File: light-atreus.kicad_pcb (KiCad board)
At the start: 2 copper layers, 40.1 x 37.5 mm, 10 parts, among them J1 USB_B, J11 USB_B, J2 CONN_01X02, J3 CONN_01X02, J4 CONN_01X02, J5 CONN_01X02, J6 CONN_01X02, J7 CONN_01X02, J8 CONN_01X02, J9 CONN_01X02

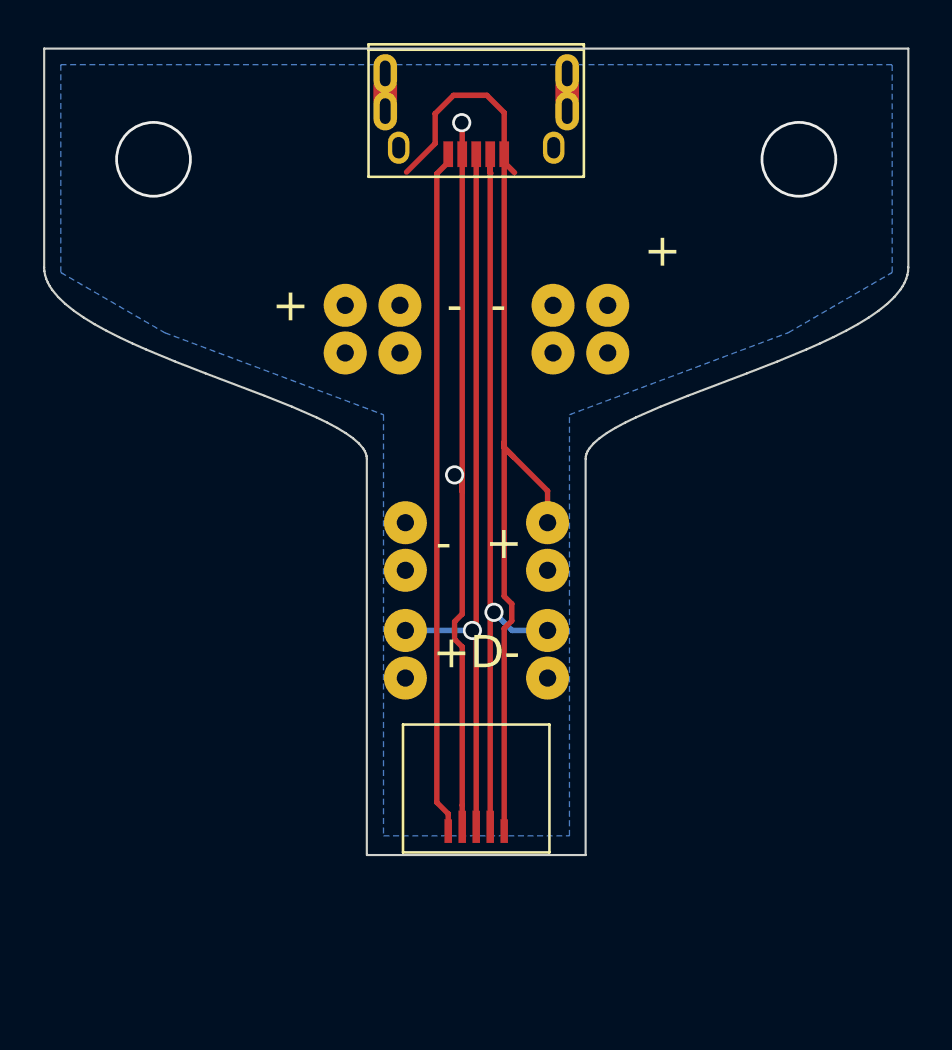
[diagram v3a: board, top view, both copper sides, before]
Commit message: Route last two V+ traces
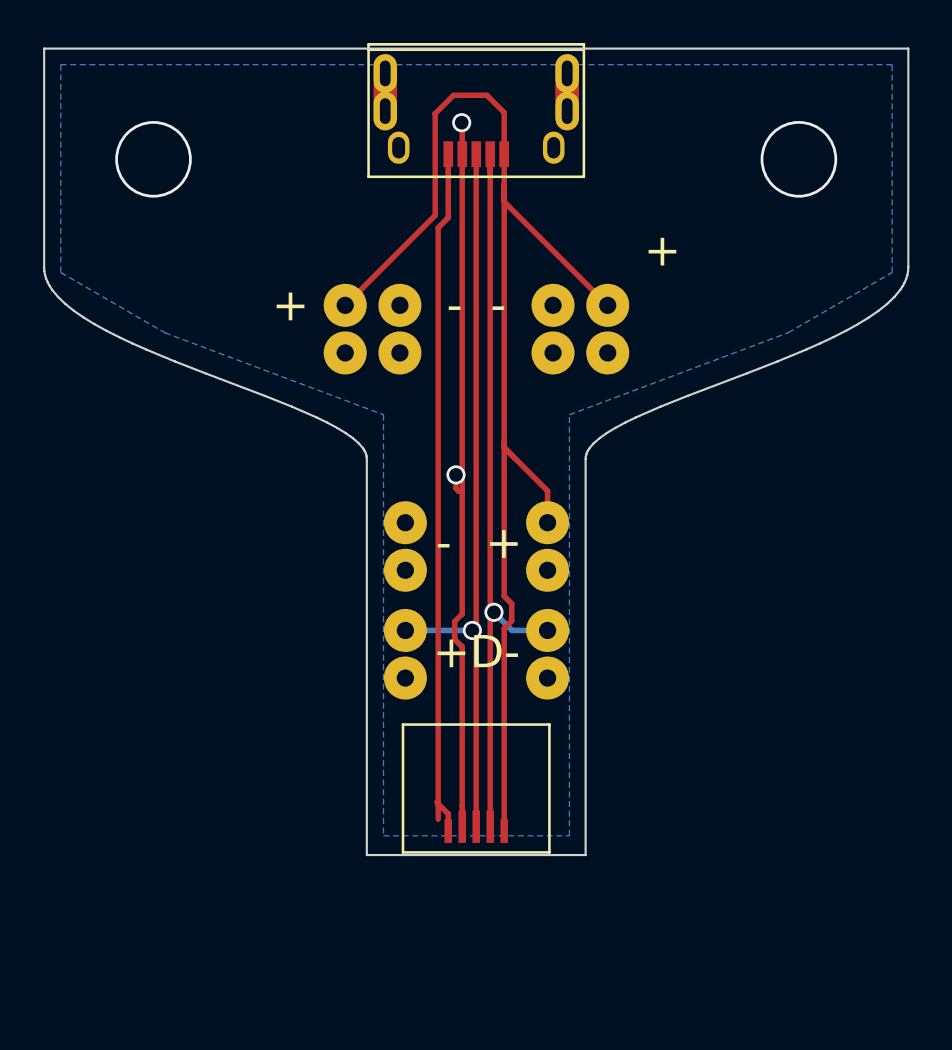
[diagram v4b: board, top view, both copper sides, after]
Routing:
- net /VBUS: track 47.4 -> 61.7 mm
- net /SHIELD: track 31.9 -> 33.0 mm
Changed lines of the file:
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@@
     (thickness 1.6)
     (drawings 74)
-    (tracks 56)
+    (tracks 60)
     (zones 0)
     (modules 10)
@@
   (via (at 145.2753 76.0222) (size 3.556) (drill 3.302) (layers F.Cu B.Cu) (net 0) (status 40000))
   (via (at 115.3033 76.0222) (size 3.556) (drill 3.302) (layers F.Cu B.Cu) (net 0) (status 40000))
+  (segment (start 128.9893 76.638) (end 128.9893 75.784) (width 0.254) (layer F.Cu) (net 1))
+  (segment (start 128.524 79.204436) (end 128.9893 78.739136) (width 0.254) (layer F.Cu) (net 1))
+  (segment (start 128.524 106.669996) (end 128.524 79.204436) (width 0.254) (layer F.Cu) (net 1))
+  (segment (start 128.9893 78.739136) (end 128.9893 76.638) (width 0.254) (layer F.Cu) (net 1))
   (segment (start 128.9893 106.4166) (end 128.9893 107.2206) (width 0.254) (layer F.Cu) (net 1))
   (segment (start 128.460498 105.887798) (end 128.9893 106.4166) (width 0.254) (layer F.Cu) (net 1))
   (segment (start 128.9893 75.784) (end 128.9893 76.159) (width 0.254) (layer F.Cu) (net 1))
-  (segment (start 128.460498 76.687802) (end 128.460498 105.887798) (width 0.254) (layer F.Cu) (net 1))
-  (segment (start 128.9893 76.159) (end 128.460498 76.687802) (width 0.254) (layer F.Cu) (net 1))
-  (segment (start 129.6393 91.0313) (end 129.286 90.678) (width 0.254) (layer F.Cu) (net 2))
+  (segment (start 129.34951 91.306617) (end 129.34951 90.678) (width 0.254) (layer F.Cu) (net 2))
+  (via (at 129.34951 90.678) (size 0.889) (drill 0.635) (layers F.Cu B.Cu) (net 2))
+  (segment (start 129.482893 91.44) (end 129.34951 91.306617) (width 0.254) (layer F.Cu) (net 2))
+  (segment (start 129.6393 91.44) (end 129.482893 91.44) (width 0.254) (layer F.Cu) (net 2))
   (segment (start 129.6393 91.44) (end 129.6393 97.139758) (width 0.254) (layer F.Cu) (net 2))
   (segment (start 129.6393 75.784) (end 129.6393 91.44) (width 0.254) (layer F.Cu) (net 2))
-  (segment (start 129.6393 91.44) (end 129.6393 91.0313) (width 0.254) (layer F.Cu) (net 2))
-  (via (at 129.286 90.678) (size 0.889) (drill 0.635) (layers F.Cu B.Cu) (net 2))
   (segment (start 129.6393 106.0166) (end 129.6393 107.0206) (width 0.254) (layer F.Cu) (net 2))
   (segment (start 129.6393 98.664242) (end 129.6393 106.0166) (width 0.254) (layer F.Cu) (net 2))
@@
   (via (at 131.11481 97.059526) (size 0.889) (drill 0.635) (layers F.Cu B.Cu) (net 4))
   (segment (start 130.9393 75.784) (end 130.9393 96.884016) (width 0.254) (layer F.Cu) (net 4))
-  (segment (start 130.9393 76.638) (end 130.975101 76.673801) (width 0.254) (layer F.Cu) (net 4))
   (segment (start 130.9393 75.784) (end 130.9393 76.638) (width 0.254) (layer F.Cu) (net 4))
-  (segment (start 131.5893 75.784) (end 131.5893 89.154) (width 0.254) (layer F.Cu) (net 5))
+  (segment (start 131.5893 75.784) (end 131.5893 73.8551) (width 0.254) (layer F.Cu) (net 5))
+  (segment (start 131.5893 73.8551) (end 130.7846 73.0504) (width 0.254) (layer F.Cu) (net 5))
+  (segment (start 128.383299 78.626701) (end 124.206 82.804) (width 0.254) (layer F.Cu) (net 5))
+  (segment (start 130.7846 73.0504) (end 129.2352 73.0504) (width 0.254) (layer F.Cu) (net 5))
+  (segment (start 129.2352 73.0504) (end 128.383299 73.902301) (width 0.254) (layer F.Cu) (net 5))
+  (segment (start 128.383299 73.902301) (end 128.383299 78.626701) (width 0.254) (layer F.Cu) (net 5))
+  (segment (start 131.5893 77.216) (end 131.5893 89.154) (width 0.254) (layer F.Cu) (net 5))
+  (segment (start 131.5893 75.784) (end 131.5893 77.216) (width 0.254) (layer F.Cu) (net 5))
+  (segment (start 131.5893 77.216) (end 131.5893 77.9953) (width 0.254) (layer F.Cu) (net 5))
+  (segment (start 131.5893 77.9953) (end 136.398 82.804) (width 0.254) (layer F.Cu) (net 5))
   (segment (start 131.5893 89.154) (end 131.5893 89.408) (width 0.254) (layer F.Cu) (net 5))
   (segment (start 131.5893 107.2206) (end 131.5893 97.806778) (width 0.254) (layer F.Cu) (net 5))
@@
   (segment (start 133.604 92.898) (end 133.604 91.4227) (width 0.254) (layer F.Cu) (net 5))
   (segment (start 133.604 91.4227) (end 131.5893 89.408) (width 0.254) (layer F.Cu) (net 5))
-  (segment (start 131.5893 73.8551) (end 131.5893 75.784) (width 0.254) (layer F.Cu) (net 5))
-  (segment (start 127.054226 76.61501) (end 128.383299 75.285937) (width 0.254) (layer F.Cu) (net 5))
-  (segment (start 128.383299 75.285937) (end 128.383299 73.902301) (width 0.254) (layer F.Cu) (net 5))
-  (segment (start 128.383299 73.902301) (end 129.2352 73.0504) (width 0.254) (layer F.Cu) (net 5))
-  (segment (start 129.2352 73.0504) (end 130.7846 73.0504) (width 0.254) (layer F.Cu) (net 5))
-  (segment (start 130.7846 73.0504) (end 131.5893 73.8551) (width 0.254) (layer F.Cu) (net 5))
-  (segment (start 131.5893 76.159) (end 132.0683 76.638) (width 0.254) (layer F.Cu) (net 5))
   (segment (start 131.5893 75.784) (end 131.5893 76.159) (width 0.254) (layer F.Cu) (net 5))
   (zone (net 2) (net_name /GND) (layer B.Cu) (hatch edge 0.508)

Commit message: Clean up ugly trace bits
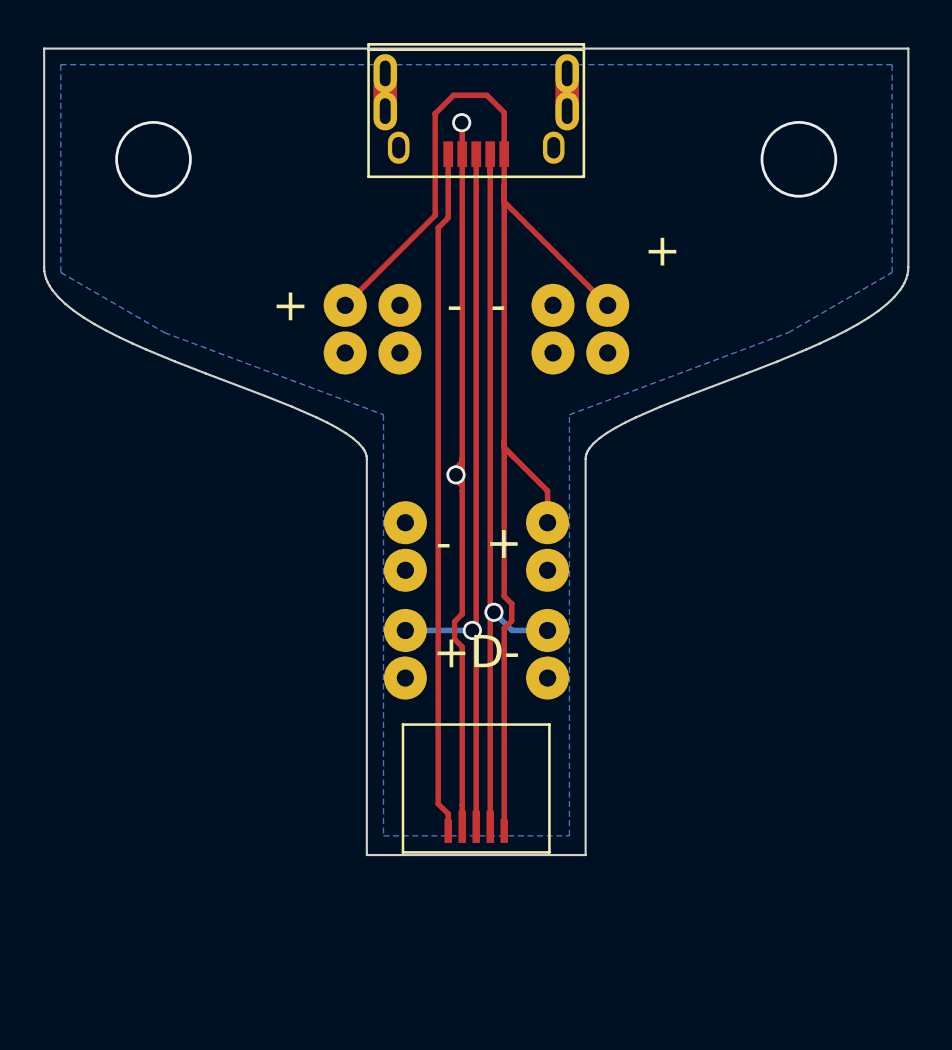
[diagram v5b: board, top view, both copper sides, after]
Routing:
- net /SHIELD: track 33.0 -> 32.2 mm
- net /GND: track 34.0 -> 34.5 mm
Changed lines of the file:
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@@
     (thickness 1.6)
     (drawings 74)
-    (tracks 60)
+    (tracks 64)
     (zones 0)
     (modules 10)
@@
   (via (at 145.2753 76.0222) (size 3.556) (drill 3.302) (layers F.Cu B.Cu) (net 0) (status 40000))
   (via (at 115.3033 76.0222) (size 3.556) (drill 3.302) (layers F.Cu B.Cu) (net 0) (status 40000))
+  (segment (start 128.9893 107.2206) (end 128.9893 106.4166) (width 0.254) (layer F.Cu) (net 1))
+  (segment (start 128.9893 106.4166) (end 128.524 105.9513) (width 0.254) (layer F.Cu) (net 1))
+  (segment (start 128.524 105.9513) (end 128.524 79.204436) (width 0.254) (layer F.Cu) (net 1))
+  (segment (start 128.524 79.204436) (end 128.9893 78.739136) (width 0.254) (layer F.Cu) (net 1))
   (segment (start 128.9893 76.638) (end 128.9893 75.784) (width 0.254) (layer F.Cu) (net 1))
-  (segment (start 128.524 79.204436) (end 128.9893 78.739136) (width 0.254) (layer F.Cu) (net 1))
-  (segment (start 128.524 106.669996) (end 128.524 79.204436) (width 0.254) (layer F.Cu) (net 1))
   (segment (start 128.9893 78.739136) (end 128.9893 76.638) (width 0.254) (layer F.Cu) (net 1))
-  (segment (start 128.9893 106.4166) (end 128.9893 107.2206) (width 0.254) (layer F.Cu) (net 1))
-  (segment (start 128.460498 105.887798) (end 128.9893 106.4166) (width 0.254) (layer F.Cu) (net 1))
   (segment (start 128.9893 75.784) (end 128.9893 76.159) (width 0.254) (layer F.Cu) (net 1))
-  (segment (start 129.34951 91.306617) (end 129.34951 90.678) (width 0.254) (layer F.Cu) (net 2))
+  (segment (start 129.6393 75.784) (end 129.6393 89.916) (width 0.254) (layer F.Cu) (net 2))
+  (segment (start 129.6393 89.916) (end 129.6393 91.186) (width 0.254) (layer F.Cu) (net 2))
+  (segment (start 129.34951 90.36049) (end 129.6393 90.0707) (width 0.254) (layer F.Cu) (net 2))
+  (segment (start 129.6393 90.0707) (end 129.6393 89.916) (width 0.254) (layer F.Cu) (net 2))
+  (segment (start 129.34951 90.678) (end 129.34951 90.36049) (width 0.254) (layer F.Cu) (net 2))
+  (segment (start 129.6393 91.186) (end 129.6393 91.44) (width 0.254) (layer F.Cu) (net 2))
+  (segment (start 129.34951 90.678) (end 129.34951 90.89621) (width 0.254) (layer F.Cu) (net 2))
+  (segment (start 129.34951 90.89621) (end 129.6393 91.186) (width 0.254) (layer F.Cu) (net 2))
   (via (at 129.34951 90.678) (size 0.889) (drill 0.635) (layers F.Cu B.Cu) (net 2))
-  (segment (start 129.482893 91.44) (end 129.34951 91.306617) (width 0.254) (layer F.Cu) (net 2))
-  (segment (start 129.6393 91.44) (end 129.482893 91.44) (width 0.254) (layer F.Cu) (net 2))
   (segment (start 129.6393 91.44) (end 129.6393 97.139758) (width 0.254) (layer F.Cu) (net 2))
-  (segment (start 129.6393 75.784) (end 129.6393 91.44) (width 0.254) (layer F.Cu) (net 2))
   (segment (start 129.6393 106.0166) (end 129.6393 107.0206) (width 0.254) (layer F.Cu) (net 2))
   (segment (start 129.6393 98.664242) (end 129.6393 106.0166) (width 0.254) (layer F.Cu) (net 2))
